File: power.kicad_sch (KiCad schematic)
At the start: 0 parts

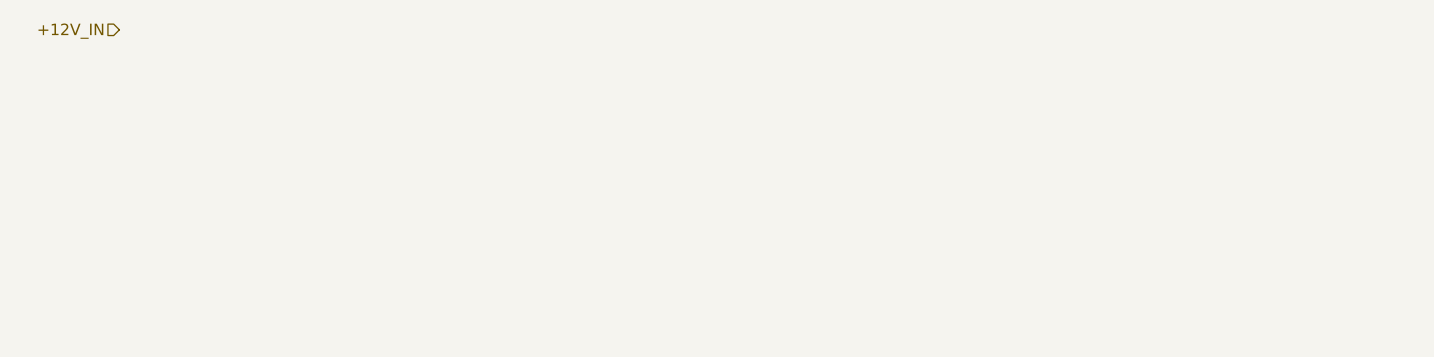
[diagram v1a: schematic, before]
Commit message: [#82147] Add notes about required power buses
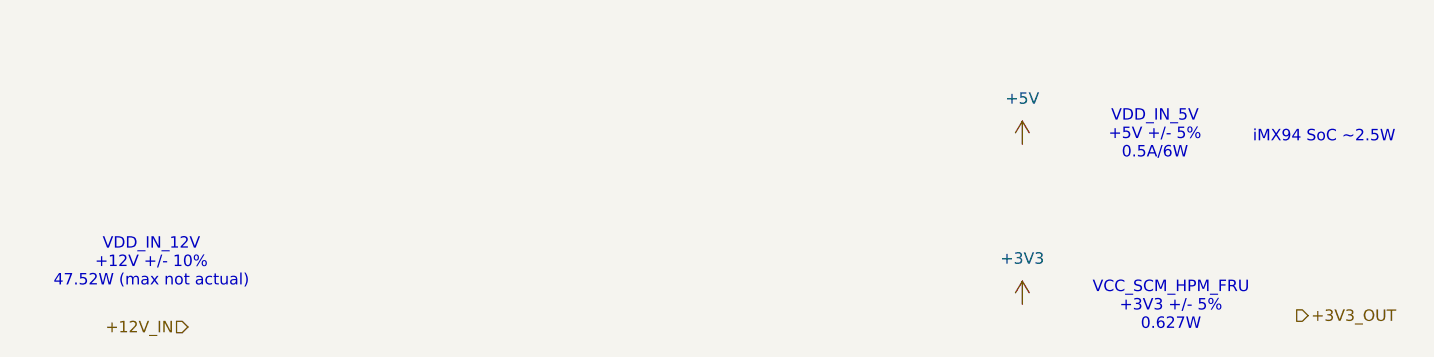
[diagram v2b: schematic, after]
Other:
- note added: "VCC_SCM_HPM_FRU +3V3 +/- 5% 0.627W"
- note added: "VDD_IN_12V +12V +/- 10% 47.52W (max not actual)"
- note added: "VDD_IN_5V +5V +/- 5% 0.5A/6W"
- note added: "iMX94 SoC ~2.5W"
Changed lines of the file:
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@@
 		(rev "1.0.0")
+	)
+	(text "VDD_IN_5V \n+5V +/- 5% \n0.5A/6W "
+		(exclude_from_sim no)
+		(at 228.092 113.284 0)
+		(effects
+			(font
+				(size 1.27 1.27)
+			)
+		)
+	)
+	(text "VCC_SCM_HPM_FRU \n+3V3 +/- 5%\n0.627W"
+		(exclude_from_sim no)
+		(at 229.87 132.334 0)
+		(effects
+			(font
+				(size 1.27 1.27)
+			)
+		)
+	)
+	(text "iMX94 SoC ~2.5W"
+		(exclude_from_sim no)
+		(at 246.888 113.538 0)
+		(effects
+			(font
+				(size 1.27 1.27)
+			)
+		)
+	)
+	(text "VDD_IN_12V\n+12V +/- 10% \n47.52W (max not actual)"
+		(exclude_from_sim no)
+		(at 116.586 127.508 0)
+		(effects
+			(font
+				(size 1.27 1.27)
+			)
+		)
 	)
 	(hierarchical_label "+12V_IN"
 		(shape input)
-		(at 113.03 101.6 180)
+		(at 120.65 134.62 180)
 		(effects
 			(font
@@
 		)
 	)
+	(hierarchical_label "+3V3_OUT"
+		(shape output)
+		(at 243.84 133.35 0)
+		(effects
+			(font
+				(size 1.27 1.27)
+			)
+			(justify left)
+		)
+	)
+	(symbol
+		(lib_id "antmicropower:+5V")
+		(at 213.36 114.3 0)
+		(unit 1)
+		(exclude_from_sim no)
+		(in_bom yes)
+		(on_board yes)
+		(dnp no)
+		(fields_autoplaced yes)
+		(property "Reference" "#PWR080"
+			(at 228.6 116.84 0)
+			(effects
+				(font
+					(size 1.27 1.27)
+					(thickness 0.15)
+				)
+				(justify left bottom)
+				(hide yes)
+			)
+		)
+		(property "Value" "+5V"
+			(at 213.36 109.22 0)
+			(effects
+				(font
+					(size 1.27 1.27)
+					(thickness 0.15)
+				)
+			)
+		)
+		(property "Footprint" ""
+			(at 228.6 121.92 0)
+			(effects
+				(font
+					(size 1.27 1.27)
+					(thickness 0.15)
+				)
+				(justify left bottom)
+				(hide yes)
+			)
+		)
+		(property "Datasheet" ""
+			(at 228.6 124.46 0)
+			(effects
+				(font
+					(size 1.27 1.27)
+					(thickness 0.15)
+				)
+				(justify left bottom)
+				(hide yes)
+			)
+		)
+		(property "Description" ""
+			(at 213.36 114.3 0)
+			(effects
+				(font
+					(size 1.27 1.27)
+				)
+				(hide yes)
+			)
+		)
+		(property "Author" "Antmicro"
+			(at 228.6 121.92 0)
+			(effects
+				(font
+					(size 1.27 1.27)
+					(thickness 0.15)
+				)
+				(justify left bottom)
+				(hide yes)
+			)
+		)
+		(property "License" "Apache-2.0"
+			(at 228.6 124.46 0)
+			(effects
+				(font
+					(size 1.27 1.27)
+					(thickness 0.15)
+				)
+				(justify left bottom)
+				(hide yes)
+			)
+		)
+		(pin "1"
+		)
+		(instances
+			(project ""
+				(path "/5f636c45-3c15-4731-8931-4625e0dab7e4/3d29c412-58cb-45c0-928a-e05b1352002d"
+					(reference "#PWR080")
+					(unit 1)
+				)
+			)
+		)
+	)
+	(symbol
+		(lib_id "antmicropower:+3V3")
+		(at 213.36 132.08 0)
+		(unit 1)
+		(exclude_from_sim no)
+		(in_bom yes)
+		(on_board yes)
+		(dnp no)
+		(fields_autoplaced yes)
+		(property "Reference" "#PWR081"
+			(at 228.6 132.08 0)
+			(effects
+				(font
+					(size 1.27 1.27)
+					(thickness 0.15)
+				)
+				(justify left bottom)
+				(hide yes)
+			)
+		)
+		(property "Value" "+3V3"
+			(at 213.36 127 0)
+			(effects
+				(font
+					(size 1.27 1.27)
+					(thickness 0.15)
+				)
+			)
+		)
+		(property "Footprint" ""
+			(at 228.6 139.7 0)
+			(effects
+				(font
+					(size 1.27 1.27)
+					(thickness 0.15)
+				)
+				(justify left bottom)
+				(hide yes)
+			)
+		)
+		(property "Datasheet" ""
+			(at 228.6 142.24 0)
+			(effects
+				(font
+					(size 1.27 1.27)
+					(thickness 0.15)
+				)
+				(justify left bottom)
+				(hide yes)
+			)
+		)
+		(property "Description" ""
+			(at 213.36 132.08 0)
+			(effects
+				(font
+					(size 1.27 1.27)
+				)
+				(hide yes)
+			)
+		)
+		(property "Author" "Antmicro"
+			(at 228.6 134.62 0)
+			(effects
+				(font
+					(size 1.27 1.27)
+					(thickness 0.15)
+				)
+				(justify left bottom)
+				(hide yes)
+			)
+		)
+		(property "License" "Apache-2.0"
+			(at 228.6 137.16 0)
+			(effects
+				(font
+					(size 1.27 1.27)
+					(thickness 0.15)
+				)
+				(justify left bottom)
+				(hide yes)
+			)
+		)
+		(pin "1"
+		)
+		(instances
+			(project ""
+				(path "/5f636c45-3c15-4731-8931-4625e0dab7e4/3d29c412-58cb-45c0-928a-e05b1352002d"
+					(reference "#PWR081")
+					(unit 1)
+				)
+			)
+		)
+	)

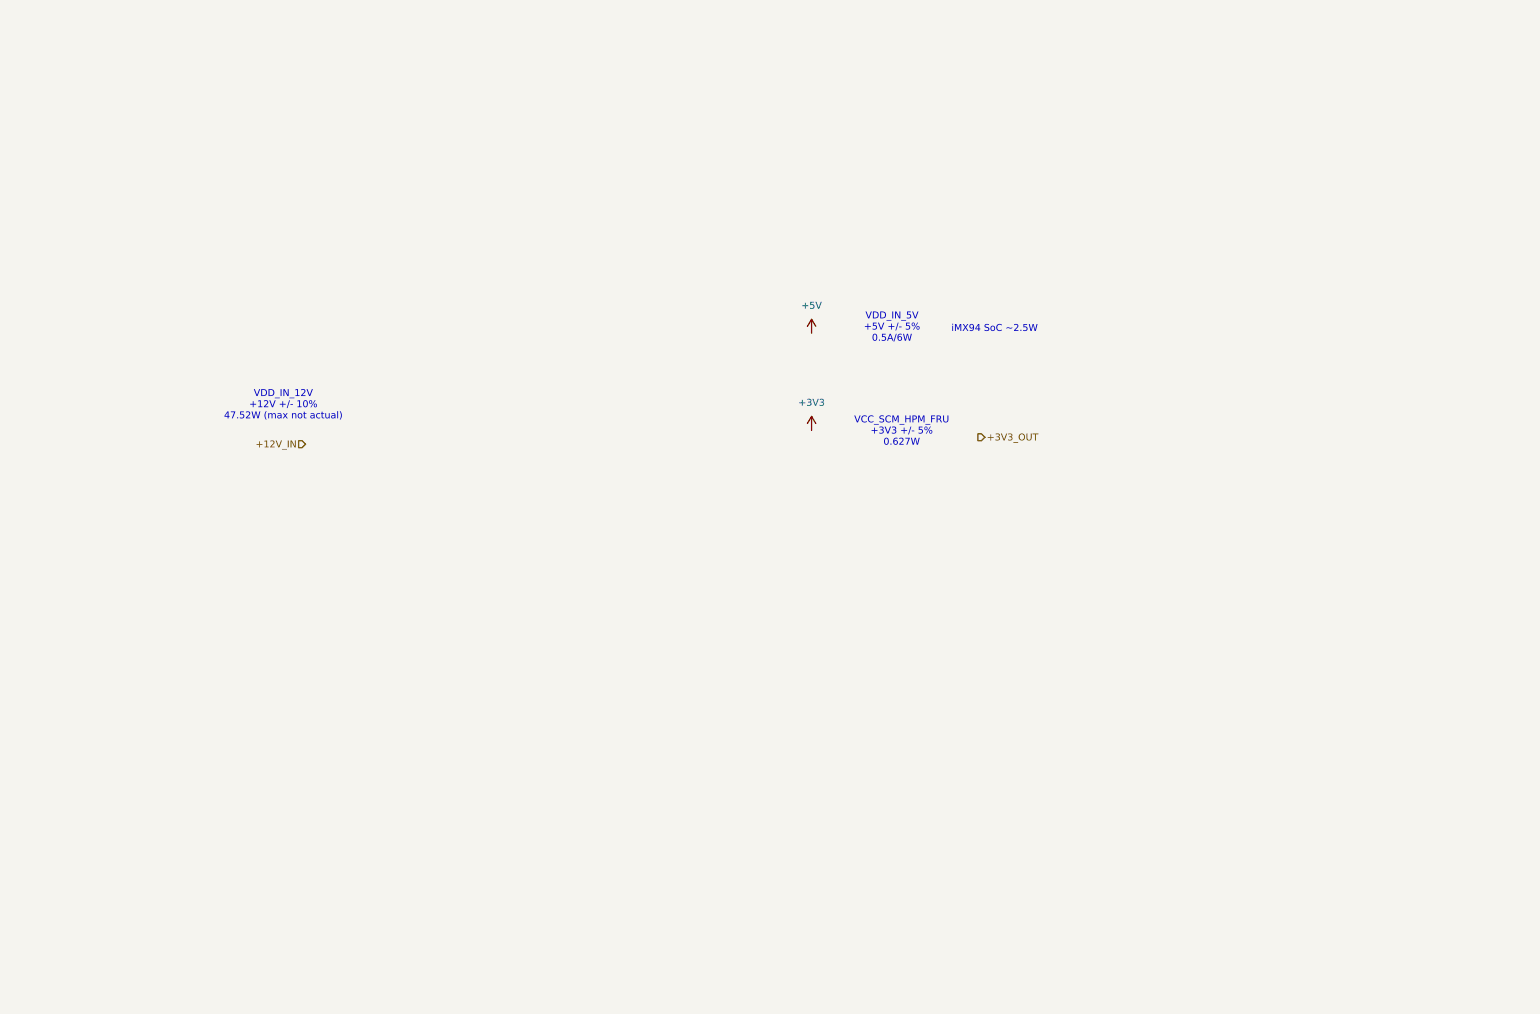
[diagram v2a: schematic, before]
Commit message: [#82147] Add 3V3 an 5V DC/DC
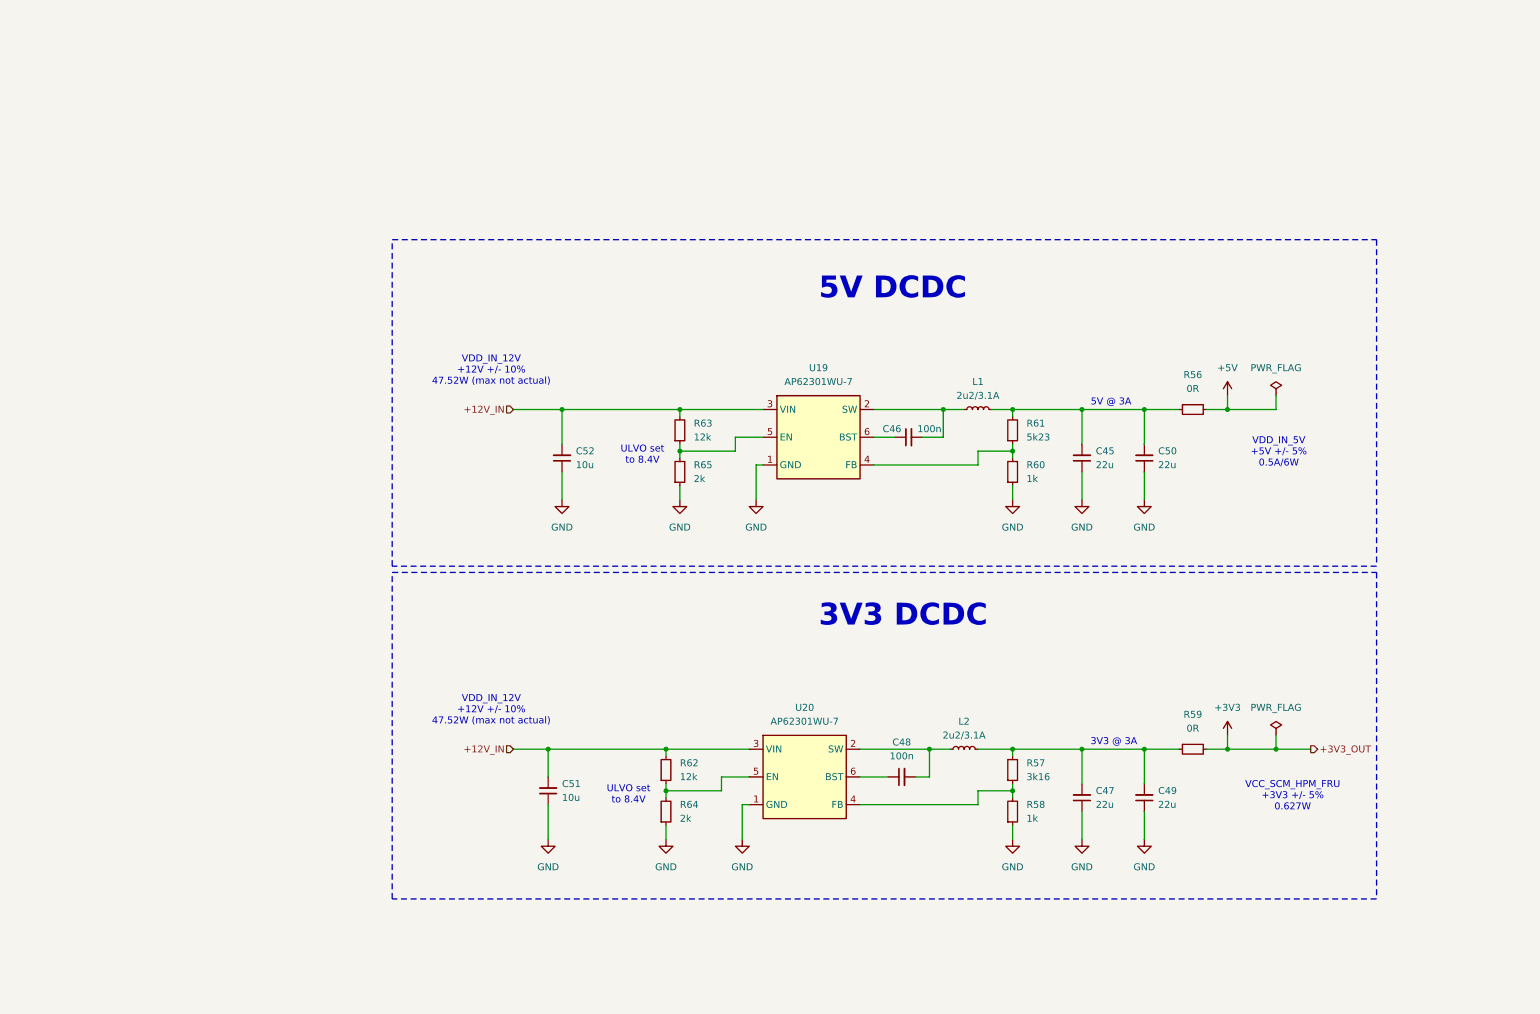
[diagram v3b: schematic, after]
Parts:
- added C45, C47, C49, C50: C_22u_0805_16V, antmicro-footprints:C_0805_2012Metric, symbol antmicroCapacitorsmisc:C_22u_0805_16V
- added C46, C48: C_100n_0402, antmicro-footprints:C_0402_1005Metric, symbol antmicroCapacitors0402:C_100n_0402
- added C51, C52: C_10u_25V_0603, antmicro-footprints:C_0603_1608Metric, symbol antmicroCapacitors0603:C_10u_25V_0603
- added L1, L2: L_2u2_3.1A_Vishay-IFSC-1515AH-01, antmicro-footprints:L_Vishay-IFSC-1515AH, symbol antmicroFixedInductors:L_2u2_3.1A_Vishay-IFSC-1515AH-01
- added R56, R59: R_0R_0402, antmicro-footprints:R_0402_1005Metric, symbol antmicroResistors0402:R_0R_0402
- added R57: R_3k16_0402, antmicro-footprints:R_0402_1005Metric, symbol antmicroResistors0402:R_3k16_0402
- added R58, R60: R_1k_0402, antmicro-footprints:R_0402_1005Metric, symbol antmicroResistors0402:R_1k_0402
- added R61: R_5k23_0402, antmicro-footprints:R_0402_1005Metric, symbol antmicroResistors0402:R_5k23_0402
- added R62, R63: R_12k_0402, antmicro-footprints:R_0402_1005Metric, symbol antmicroResistors0402:R_12k_0402
- added R64, R65: R_2k_0402, antmicro-footprints:R_0402_1005Metric, symbol antmicroResistors0402:R_2k_0402
- added U19, U20: AP62301_TSOT, antmicro-footprints:TSOT23-6, symbol antmicroDCDCConverters:AP62301_TSOT
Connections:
- net +12V_IN: now also C51.2, C52.2, R62.2, R63.2, U19.3 (VIN), U20.3 (VIN)
- net +3V3: now also R59.2
- net +5V: now also R56.2
- new net: C45.2, C50.2, L1.2, R56.1, R61.2
- new net: C46.2, L1.1, U19.2 (SW)
- new net: R60.2, R61.1, U19.4 (FB)
- new net: R63.1, R65.2, U19.5 (EN)
- new net: C46.1, U19.6 (BST)
- new net: C48.2, L2.1, U20.2 (SW)
- new net: R57.1, R58.2, U20.4 (FB)
- new net: R62.1, R64.2, U20.5 (EN)
- new net: C48.1, U20.6 (BST)
- new net: C47.2, C49.2, L2.2, R57.2, R59.1
- new net GND: C45.1, C47.1, C49.1, C50.1, C51.1, C52.1, R58.1, R60.1, R64.1, R65.1, U19.1 (GND), U20.1 (GND)
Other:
- note added: "3V3 @ 3A"
- note added: "3V3 DCDC"
- note added: "5V @ 3A"
- note added: "5V DCDC"
- note added: "ULVO set to 8.4V"
- note removed: "iMX94 SoC ~2.5W"

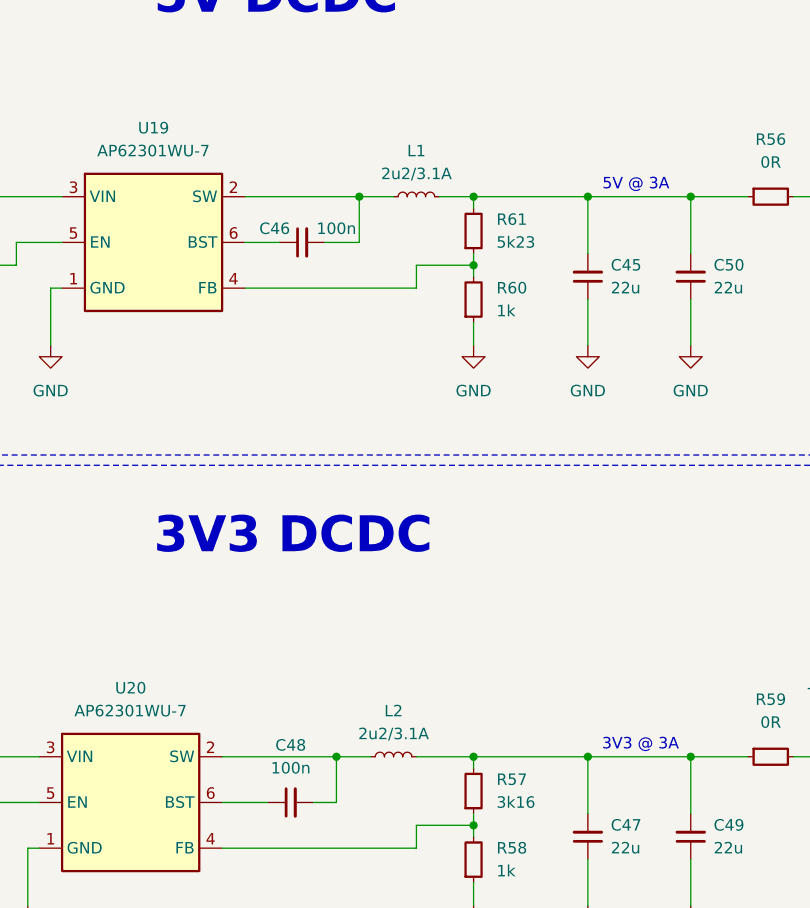
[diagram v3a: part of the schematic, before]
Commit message: [#82190] Change DC/DC coils to SRP3212A
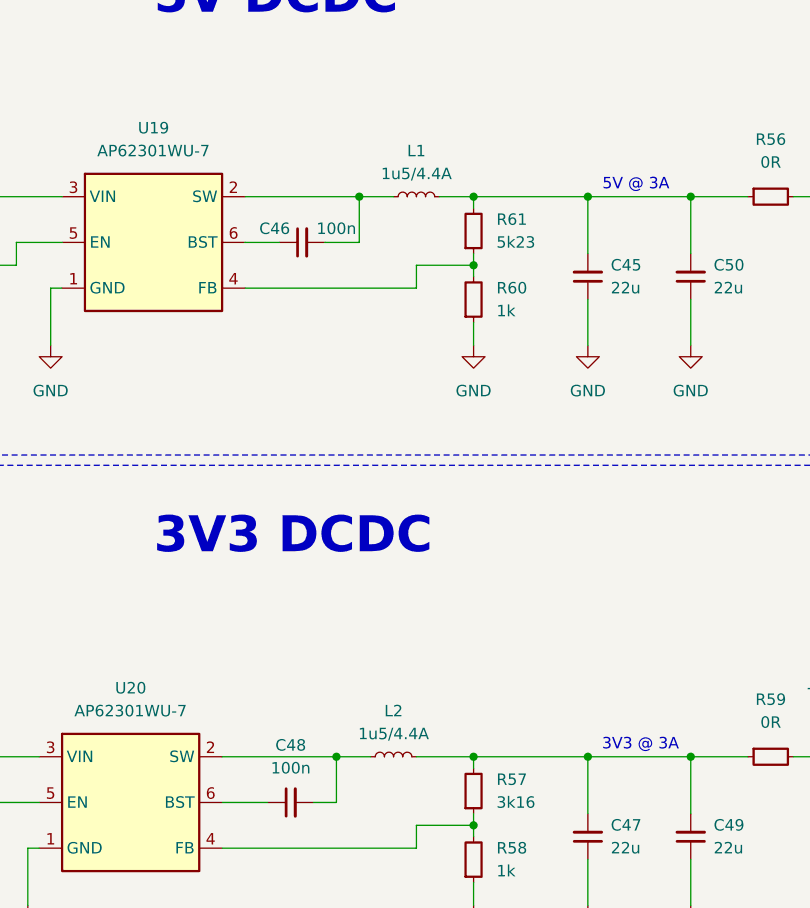
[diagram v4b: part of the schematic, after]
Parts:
- removed L1, L2: L_2u2_3.1A_Vishay-IFSC-1515AH-01, antmicro-footprints:L_Vishay-IFSC-1515AH, symbol antmicroFixedInductors:L_2u2_3.1A_Vishay-IFSC-1515AH-01
- added L1, L2: L_1u5_4.4A_Bourns-SRP3212A, antmicro-footprints:L_Bourns-SRP3212A, symbol antmicroFixedInductors:L_1u5_4.4A_Bourns-SRP3212A
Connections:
- net at C45.2, C50.2, R56.1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: now also L1.2
- net at C46.2, U19.2 (SW): now also L1.1
- net at C48.2, U20.2 (SW): now also L2.1
- net at C47.2, C49.2, R57.2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: now also L2.2

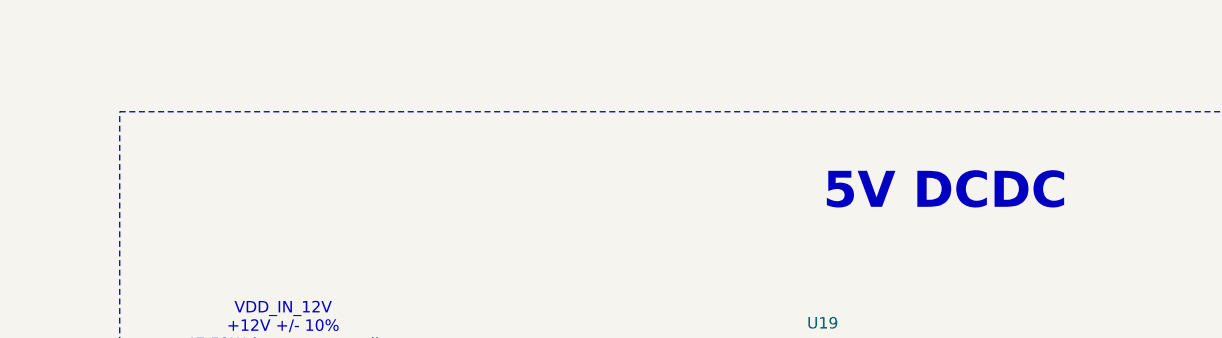
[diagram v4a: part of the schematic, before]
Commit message: [#83146] Set LTPI bias voltage
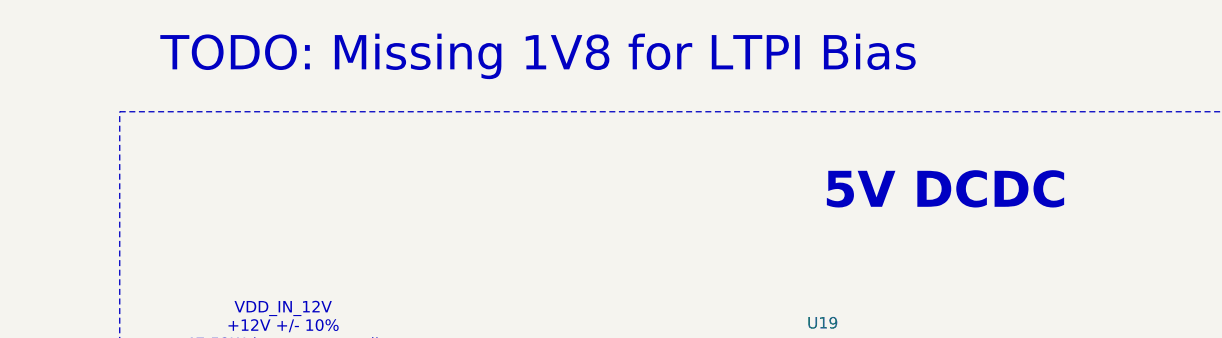
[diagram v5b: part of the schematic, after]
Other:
- note added: "TODO: Missing 1V8 for LTPI Bias"
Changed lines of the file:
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@@
+		)
+	)
+	(text "TODO: Missing 1V8 for LTPI Bias"
+		(exclude_from_sim no)
+		(at 183.134 90.932 0)
+		(effects
+			(font
+				(size 3.81 3.81)
+			)
 		)
 	)
